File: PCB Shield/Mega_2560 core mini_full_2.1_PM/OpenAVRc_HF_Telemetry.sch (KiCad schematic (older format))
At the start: 12 parts, among them P18 Ecolage, P19 Module_TX, P20 TTL/RS232, P7 SPIX, U1 74LVC1G3157GV, U2 TLP290, U3 TLP290

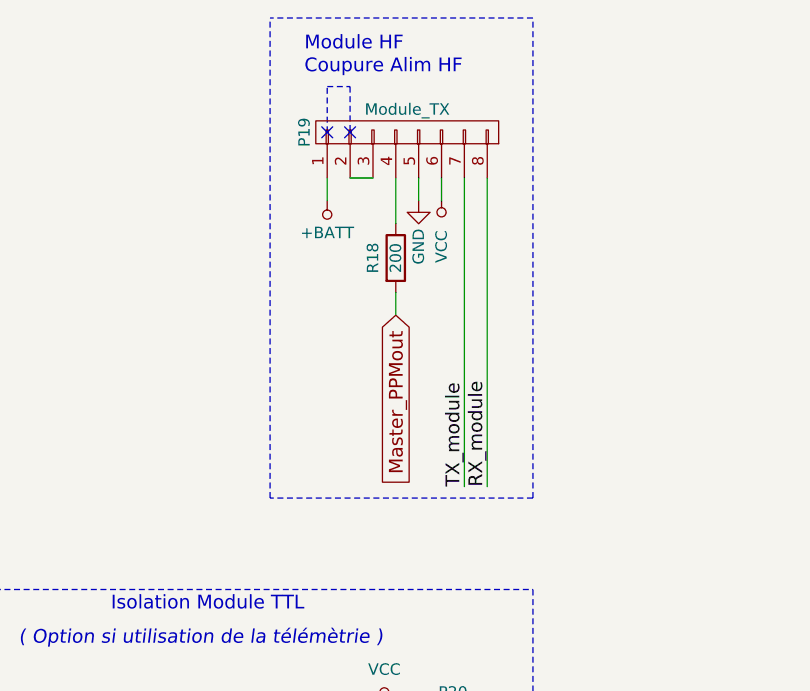
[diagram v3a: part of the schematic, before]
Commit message: Update schematic & pcb
-modify P19 pinout
-connect Q1 to B7 pin's core
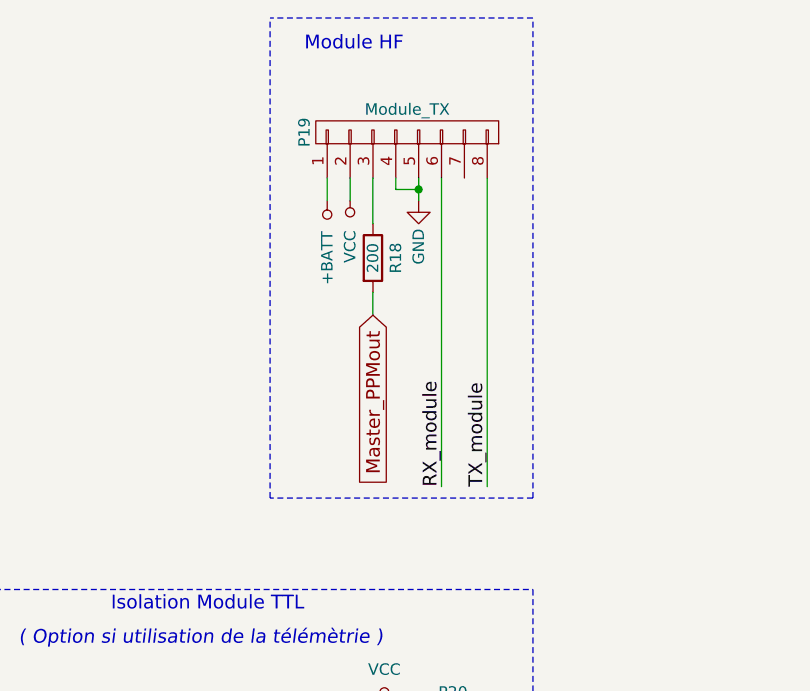
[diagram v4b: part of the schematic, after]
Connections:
- net GND: now also P19.4 (P4)
- net RX_module: now also P19.6 (P6); no longer P19.8 (P8)
- net TX_module: now also P19.8 (P8); no longer P19.7 (P7)
- net VCC: now also P19.2 (P2); no longer P19.6 (P6)
- net at P19.3 (P3): now also R18.1; no longer P19.2 (P2)
- no-connect marks 2 -> 0
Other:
- note removed: "Coupure Alim HF"
- moved on the sheet: R18
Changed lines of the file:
@@
 Sheet 4 7
 Title "Shield Mega2560 core Full"
-Date "2018-02-03"
+Date "2018-02-14"
 Rev "2.10"
 Comp "© Team OpenAVRc"
@@
 $EndComp
 $Comp
-L GND-RESCUE-Mega_2560_core_mini_full_2.0 #PWR66
+L GND-RESCUE-Mega_2560_core_mini_full_2.0 #PWR067
 U 1 1 59C6B422
 P 1850 5200
-F 0 "#PWR66" H 1850 4950 50  0001 C CNN
+F 0 "#PWR067" H 1850 4950 50  0001 C CNN
 F 1 "GND" H 1850 5050 50  0000 C CNN
 F 2 "" H 1850 5200 50  0000 C CNN
@@
 $EndComp
 $Comp
-L +BATT #PWR65
+L +BATT #PWR068
 U 1 1 59C6B429
 P 1600 4100
-F 0 "#PWR65" H 1600 3950 50  0001 C CNN
+F 0 "#PWR068" H 1600 3950 50  0001 C CNN
 F 1 "+BATT" H 1600 4240 50  0000 C CNN
 F 2 "" H 1600 4100 50  0000 C CNN
@@
 $EndComp
 $Comp
-L GND-RESCUE-Mega_2560_core_mini_full_2.0 #PWR70
+L GND-RESCUE-Mega_2560_core_mini_full_2.0 #PWR069
 U 1 1 59C6B436
 P 3850 2000
-F 0 "#PWR70" H 3850 1750 50  0001 C CNN
+F 0 "#PWR069" H 3850 1750 50  0001 C CNN
 F 1 "GND" V 3850 1800 50  0000 C CNN
 F 2 "" H 3850 2000 50  0000 C CNN
@@
 $EndComp
 $Comp
-L VCC #PWR71
+L VCC #PWR070
 U 1 1 59C6B43D
-P 3950 2000
-F 0 "#PWR71" H 3950 1850 50  0001 C CNN
-F 1 "VCC" V 3950 2200 50  0000 C CNN
-F 2 "" H 3950 2000 50  0000 C CNN
-F 3 "" H 3950 2000 50  0000 C CNN
-	1    3950 2000
+P 3550 2000
+F 0 "#PWR070" H 3550 1850 50  0001 C CNN
+F 1 "VCC" V 3550 2200 50  0000 C CNN
+F 2 "" H 3550 2000 50  0000 C CNN
+F 3 "" H 3550 2000 50  0000 C CNN
+	1    3550 2000
 	-1   0    0    1
 $EndComp
@@
 Isolation Module TTL
 $Comp
-L +BATT #PWR67
+L +BATT #PWR071
 U 1 1 59C6B445
 P 3450 2000
-F 0 "#PWR67" H 3450 1850 50  0001 C CNN
-F 1 "+BATT" H 3450 2140 50  0000 C CNN
+F 0 "#PWR071" H 3450 1850 50  0001 C CNN
+F 1 "+BATT" V 3450 2250 50  0000 C CNN
 F 2 "" H 3450 2000 50  0000 C CNN
 F 3 "" H 3450 2000 50  0000 C CNN
@@
 	-1   0    0    1
 $EndComp
-NoConn ~ 3450 1700
-NoConn ~ 3550 1700
 $Comp
 L R-RESCUE-Mega_2560_core_mini_full_2.0 R8
@@
 $EndComp
 $Comp
-L GND-RESCUE-Mega_2560_core_mini_full_2.0 #PWR78
+L GND-RESCUE-Mega_2560_core_mini_full_2.0 #PWR072
 U 1 1 59C6B464
 P 9650 5100
-F 0 "#PWR78" H 9650 4850 50  0001 C CNN
+F 0 "#PWR072" H 9650 4850 50  0001 C CNN
 F 1 "GND" H 9650 4950 50  0000 C CNN
 F 2 "" H 9650 5100 50  0000 C CNN
@@
 $EndComp
 $Comp
-L GND-RESCUE-Mega_2560_core_mini_full_2.0 #PWR69
+L GND-RESCUE-Mega_2560_core_mini_full_2.0 #PWR073
 U 1 1 59C6B478
 P 3750 5000
-F 0 "#PWR69" H 3750 4750 50  0001 C CNN
+F 0 "#PWR073" H 3750 4750 50  0001 C CNN
 F 1 "GND" H 3750 4850 50  0000 C CNN
 F 2 "" H 3750 5000 50  0000 C CNN
@@
 $EndComp
 $Comp
-L VCC #PWR68
+L VCC #PWR074
 U 1 1 59C6B47E
 P 3700 4200
-F 0 "#PWR68" H 3700 4050 50  0001 C CNN
+F 0 "#PWR074" H 3700 4050 50  0001 C CNN
 F 1 "VCC" H 3700 4350 50  0000 C CNN
 F 2 "" H 3700 4200 50  0000 C CNN
@@
 	1    0    0    -1
 $EndComp
-Text Notes 3350 1450 0    60   ~ 0
-Coupure Alim HF
 Text Label 3200 4350 0    60   ~ 0
 TX_module
@@
 RX_module
 Text Label 4150 3250 1    60   ~ 0
+TX_module
+Text Label 3950 3250 1    60   ~ 0
 RX_module
-Text Label 4050 3250 1    60   ~ 0
-TX_module
 $Comp
 L 74LVC1G3157 U1
@@
 $EndComp
 $Comp
-L VCC #PWR77
+L VCC #PWR075
 U 1 1 59C6B497
 P 8800 4500
-F 0 "#PWR77" H 8800 4350 50  0001 C CNN
+F 0 "#PWR075" H 8800 4350 50  0001 C CNN
 F 1 "VCC" H 8800 4650 50  0000 C CNN
 F 2 "" H 8800 4500 50  0000 C CNN
@@
 $EndComp
 $Comp
-L GND-RESCUE-Mega_2560_core_mini_full_2.0 #PWR75
+L GND-RESCUE-Mega_2560_core_mini_full_2.0 #PWR076
 U 1 1 59C6B49D
 P 7350 4500
-F 0 "#PWR75" H 7350 4250 50  0001 C CNN
+F 0 "#PWR076" H 7350 4250 50  0001 C CNN
 F 1 "GND" H 7350 4350 50  0000 C CNN
 F 2 "" H 7350 4500 50  0000 C CNN
@@
 Wire Notes Line
 	1450 5450 4350 5450
-Wire Wire Line
-	3650 1900 3550 1900
 Connection ~ 1850 5000
 Wire Wire Line
@@
 	4150 1900 4150 3250
 Wire Wire Line
-	4050 1900 4050 3250
+	3950 1900 3950 3250
 Wire Wire Line
 	3750 4550 3800 4550
@@
 	1450 5450 1450 3700
 Wire Notes Line
-	3450 1700 3450 1500
-Wire Notes Line
-	3450 1500 3550 1500
-Wire Notes Line
-	3550 1500 3550 1700
-Wire Notes Line
 	4350 1200 3200 1200
 Wire Wire Line
@@
 Wire Wire Line
 	3750 4950 3800 4950
-Wire Wire Line
-	3950 2000 3950 1900
 Wire Wire Line
 	3850 2000 3850 1900
@@
 $EndComp
 $Comp
-L GND-RESCUE-Mega_2560_core_mini_full_2.0 #PWR76
+L GND-RESCUE-Mega_2560_core_mini_full_2.0 #PWR077
 U 1 1 59C6C686
 P 7550 2200
-F 0 "#PWR76" H 7550 1950 50  0001 C CNN
+F 0 "#PWR077" H 7550 1950 50  0001 C CNN
 F 1 "GND" H 7550 2050 50  0000 C CNN
 F 2 "" H 7550 2200 50  0000 C CNN
@@
 $EndComp
 $Comp
-L GND-RESCUE-Mega_2560_core_mini_full_2.0 #PWR73
+L GND-RESCUE-Mega_2560_core_mini_full_2.0 #PWR078
 U 1 1 59C6C68C
 P 7250 1850
-F 0 "#PWR73" H 7250 1600 50  0001 C CNN
+F 0 "#PWR078" H 7250 1600 50  0001 C CNN
 F 1 "GND" H 7250 1700 50  0000 C CNN
 F 2 "" H 7250 1850 50  0000 C CNN
@@
 $EndComp
 $Comp
-L VCC #PWR74
+L VCC #PWR079
 U 1 1 59C6C694
 P 7350 2000
-F 0 "#PWR74" H 7350 1850 50  0001 C CNN
+F 0 "#PWR079" H 7350 1850 50  0001 C CNN
 F 1 "VCC" V 7350 2150 50  0000 C CNN
 F 2 "" H 7350 2000 50  0000 C CNN
@@
 Sim_control
 $Comp
-L +3,3V #PWR72
+L +3,3V #PWR080
 U 1 1 59CA7757
 P 7050 1950
-F 0 "#PWR72" H 7050 1910 30  0001 C CNN
+F 0 "#PWR080" H 7050 1910 30  0001 C CNN
 F 1 "+3,3V" V 7050 2150 39  0000 C CNN
 F 2 "" H 7050 1950 60  0001 C CNN
@@
 L R-RESCUE-Mega_2560_core_mini_full_2.0 R18
 U 1 1 5A718C98
-P 3750 2250
-F 0 "R18" V 3650 2250 50  0000 C CNN
-F 1 "200" V 3750 2250 50  0000 C CNN
-F 2 "Resistors_SMD:R_1206" V 3680 2250 50  0001 C CNN
-F 3 "" H 3750 2250 50  0000 C CNN
-	1    3750 2250
-	1    0    0    -1
-$EndComp
-Wire Wire Line
-	3750 2100 3750 1900
+P 3650 2250
+F 0 "R18" V 3750 2250 50  0000 C CNN
+F 1 "200" V 3650 2250 50  0000 C CNN
+F 2 "Resistors_SMD:R_1206" V 3580 2250 50  0001 C CNN
+F 3 "" H 3650 2250 50  0000 C CNN
+	1    3650 2250
+	1    0    0    -1
+$EndComp
 $Comp
 L R-RESCUE-Mega_2560_core_mini_full_2.0 R19
@@
 Wire Wire Line
 	2650 5000 2550 5000
-Text GLabel 3750 2500 3    60   Input ~ 0
+Text GLabel 3650 2500 3    60   Input ~ 0
 Master_PPMout
 Wire Wire Line
-	3750 2500 3750 2400
+	3650 2500 3650 2400
 Wire Notes Line
 	4350 3300 3200 3300
@@
 Wire Notes Line
 	3200 3300 3200 1200
+Wire Wire Line
+	3650 2100 3650 1900
+Connection ~ 3850 1950
+Wire Wire Line
+	3550 2000 3550 1900
+Wire Wire Line
+	3750 1900 3750 1950
+Wire Wire Line
+	3750 1950 3850 1950
 $EndSCHEMATC

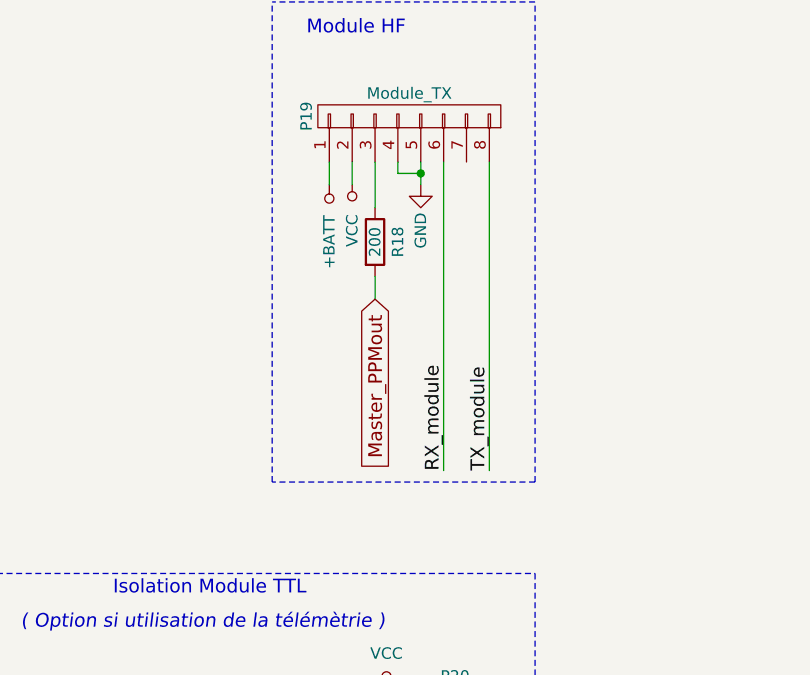
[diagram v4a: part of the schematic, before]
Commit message: Update schemtaic & PCB files
-update P19 pinout .
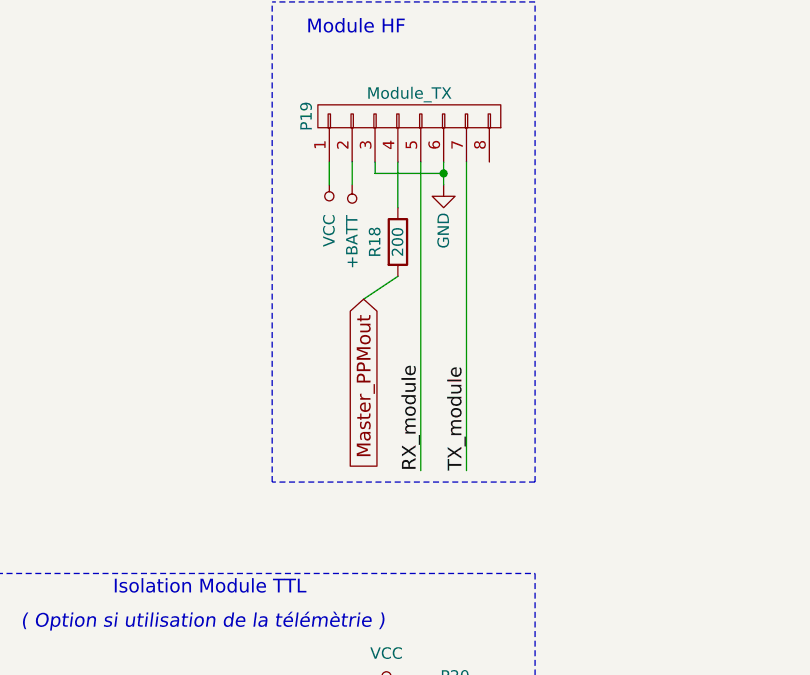
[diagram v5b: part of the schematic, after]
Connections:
- net +BATT: now also P19.2 (P2); no longer P19.1 (P1)
- net GND: now also P19.3 (P3), P19.6 (P6); no longer P19.4 (P4), P19.5 (P5)
- net RX_module: now also P19.5 (P5); no longer P19.6 (P6)
- net TX_module: now also P19.7 (P7); no longer P19.8 (P8)
- net VCC: now also P19.1 (P1); no longer P19.2 (P2)
- net at R18.1: now also P19.4 (P4); no longer P19.3 (P3)
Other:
- moved on the sheet: R18
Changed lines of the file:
@@
 Sheet 4 7
 Title "Shield Mega2560 core Full"
-Date "2018-02-14"
+Date "2018-02-15"
 Rev "2.10"
 Comp "© Team OpenAVRc"
@@
 L GND-RESCUE-Mega_2560_core_mini_full_2.0 #PWR069
 U 1 1 59C6B436
-P 3850 2000
-F 0 "#PWR069" H 3850 1750 50  0001 C CNN
-F 1 "GND" V 3850 1800 50  0000 C CNN
-F 2 "" H 3850 2000 50  0000 C CNN
-F 3 "" H 3850 2000 50  0000 C CNN
-	1    3850 2000
+P 3950 2000
+F 0 "#PWR069" H 3950 1750 50  0001 C CNN
+F 1 "GND" V 3950 1800 50  0000 C CNN
+F 2 "" H 3950 2000 50  0000 C CNN
+F 3 "" H 3950 2000 50  0000 C CNN
+	1    3950 2000
 	1    0    0    -1
 $EndComp
@@
 L VCC #PWR070
 U 1 1 59C6B43D
+P 3450 2000
+F 0 "#PWR070" H 3450 1850 50  0001 C CNN
+F 1 "VCC" V 3450 2200 50  0000 C CNN
+F 2 "" H 3450 2000 50  0000 C CNN
+F 3 "" H 3450 2000 50  0000 C CNN
+	1    3450 2000
+	-1   0    0    1
+$EndComp
+Text Notes 3350 3800 2    60   ~ 0
+Isolation Module TTL
+$Comp
+L +BATT #PWR071
+U 1 1 59C6B445
 P 3550 2000
-F 0 "#PWR070" H 3550 1850 50  0001 C CNN
-F 1 "VCC" V 3550 2200 50  0000 C CNN
+F 0 "#PWR071" H 3550 1850 50  0001 C CNN
+F 1 "+BATT" V 3550 2250 50  0000 C CNN
 F 2 "" H 3550 2000 50  0000 C CNN
 F 3 "" H 3550 2000 50  0000 C CNN
 	1    3550 2000
-	-1   0    0    1
-$EndComp
-Text Notes 3350 3800 2    60   ~ 0
-Isolation Module TTL
-$Comp
-L +BATT #PWR071
-U 1 1 59C6B445
-P 3450 2000
-F 0 "#PWR071" H 3450 1850 50  0001 C CNN
-F 1 "+BATT" V 3450 2250 50  0000 C CNN
-F 2 "" H 3450 2000 50  0000 C CNN
-F 3 "" H 3450 2000 50  0000 C CNN
-	1    3450 2000
 	-1   0    0    1
 $EndComp
@@
 Text Label 3200 4250 0    60   ~ 0
 RX_module
-Text Label 4150 3250 1    60   ~ 0
+Text Label 4050 3250 1    60   ~ 0
 TX_module
-Text Label 3950 3250 1    60   ~ 0
+Text Label 3850 3250 1    60   ~ 0
 RX_module
 $Comp
@@
 	2600 4300 2550 4300
 Wire Wire Line
-	4150 1900 4150 3250
-Wire Wire Line
-	3950 1900 3950 3250
+	4050 1900 4050 3250
+Wire Wire Line
+	3850 1900 3850 3250
 Wire Wire Line
 	3750 4550 3800 4550
@@
 	3750 4950 3800 4950
 Wire Wire Line
-	3850 2000 3850 1900
-Wire Wire Line
-	3450 2000 3450 1900
+	3550 2000 3550 1900
 $Comp
 L C-RESCUE-Mega_2560_core_mini_full_2.0 C6
@@
 L R-RESCUE-Mega_2560_core_mini_full_2.0 R18
 U 1 1 5A718C98
-P 3650 2250
-F 0 "R18" V 3750 2250 50  0000 C CNN
-F 1 "200" V 3650 2250 50  0000 C CNN
-F 2 "Resistors_SMD:R_1206" V 3580 2250 50  0001 C CNN
-F 3 "" H 3650 2250 50  0000 C CNN
-	1    3650 2250
+P 3750 2250
+F 0 "R18" V 3650 2250 50  0000 C CNN
+F 1 "200" V 3750 2250 50  0000 C CNN
+F 2 "Resistors_SMD:R_1206" V 3680 2250 50  0001 C CNN
+F 3 "" H 3750 2250 50  0000 C CNN
+	1    3750 2250
 	1    0    0    -1
 $EndComp
@@
 Wire Wire Line
 	2650 5000 2550 5000
-Text GLabel 3650 2500 3    60   Input ~ 0
+Text GLabel 3600 2500 3    60   Input ~ 0
 Master_PPMout
 Wire Wire Line
-	3650 2500 3650 2400
+	3600 2500 3750 2400
 Wire Notes Line
 	4350 3300 3200 3300
@@
 	3200 3300 3200 1200
 Wire Wire Line
-	3650 2100 3650 1900
-Connection ~ 3850 1950
-Wire Wire Line
-	3550 2000 3550 1900
-Wire Wire Line
-	3750 1900 3750 1950
-Wire Wire Line
-	3750 1950 3850 1950
+	3750 2100 3750 1900
+Wire Wire Line
+	3450 2000 3450 1900
+Wire Wire Line
+	3650 1950 3950 1950
+Wire Wire Line
+	3950 1900 3950 2000
+Connection ~ 3950 1950
+Wire Wire Line
+	3650 1950 3650 1900
 $EndSCHEMATC

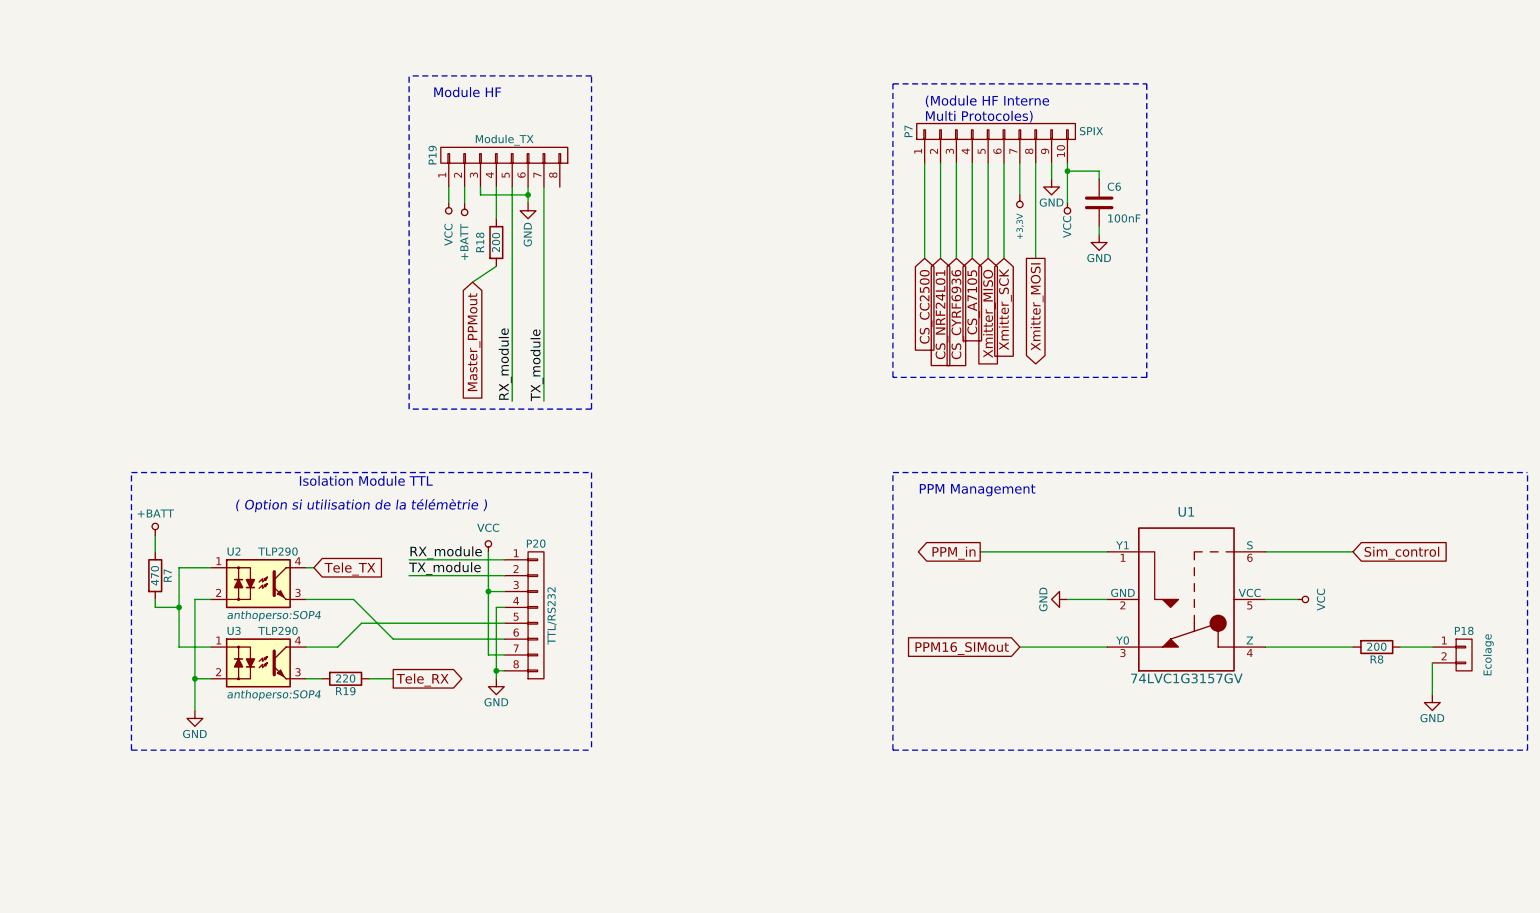
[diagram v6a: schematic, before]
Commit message: Update schematic é pcb files
-replace u2 and u3 by 2 74lvc1g3157gv
-remove p15 and p3
-add ftdi connector as p3
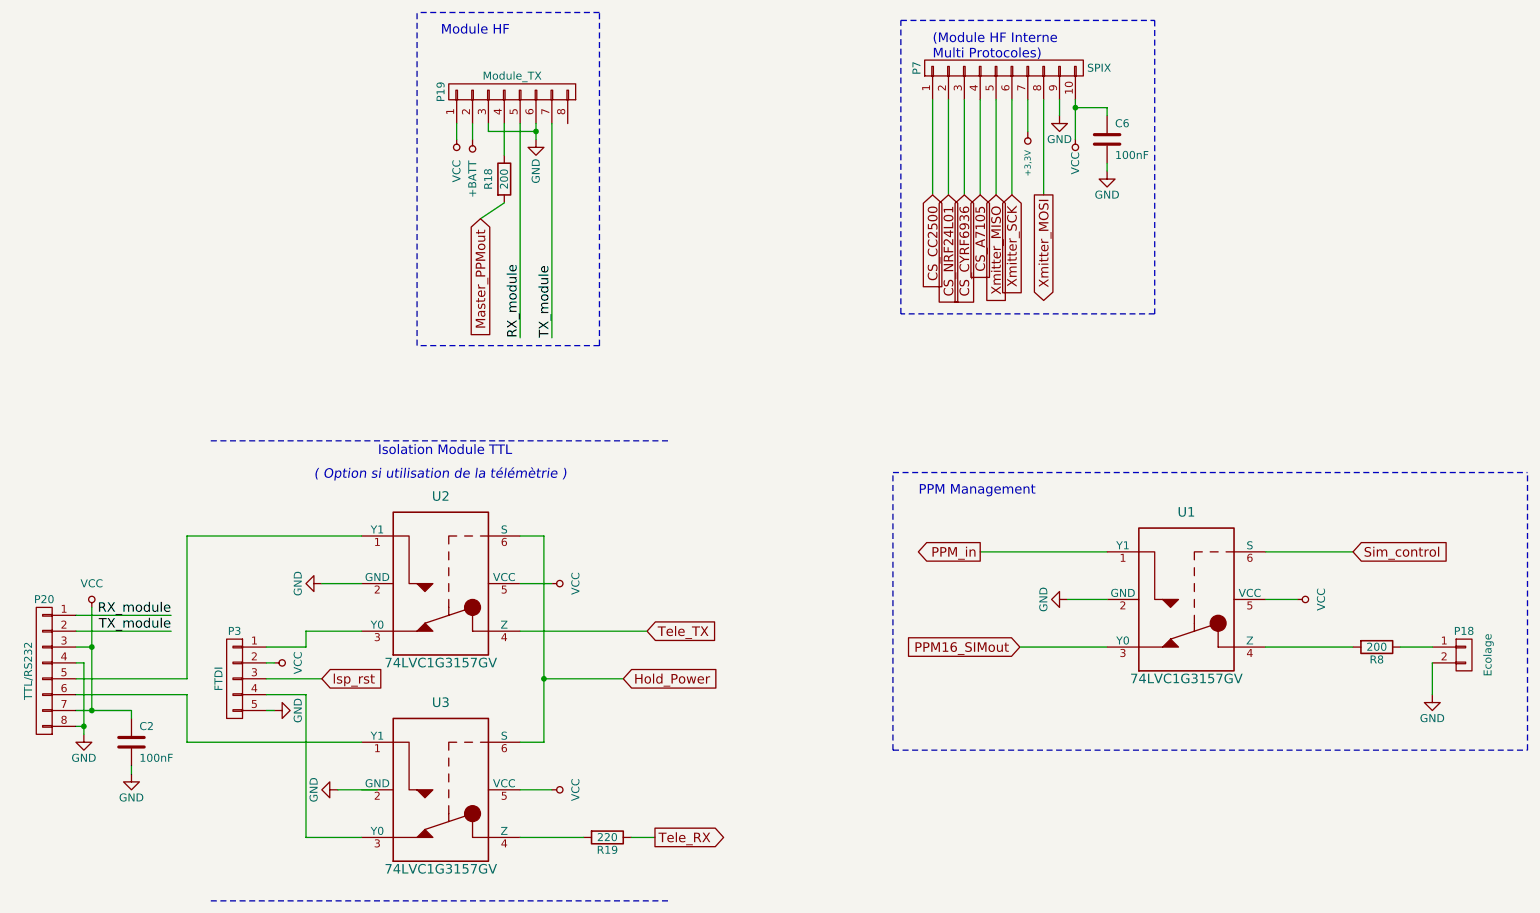
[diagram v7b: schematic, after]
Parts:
- removed R7: 470, Resistors_SMD:R_1206, symbol R-RESCUE-Mega_2560_core_mini_full_2.0
- removed U2, U3: TLP290, anthoperso:SOP4, symbol TLP290-RESCUE-Mega_2560_core_mini_full_2.0
- added C2: 100nF, Capacitors_SMD:C_1206, symbol C-RESCUE-Mega_2560_core_mini_full_2.0
- added P3: FTDI, symbol CONN_01X05
- added U2, U3: 74LVC1G3157GV, SOT-457, symbol 74LVC1G3157
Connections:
- net GND: now also C2.2, P3.5 (P5), U2.2 (GND)
- net Tele_TX: now also U2.4 (Z)
- net VCC: now also C2.1, P3.2 (P2), U2.5 (VCC), U3.5 (VCC)
- net at R19.2: now also U3.4 (Z)
- net at P20.5 (P5): now also U2.1 (Y1)
- net at P20.6 (P6): now also U3.1 (Y1)
- new net: P3.1 (P1), U2.3 (Y0)
- new net: P3.4 (P4), U3.3 (Y0)
- new net Hold_Power: U2.6 (S), U3.6 (S)
- new net lsp_rst: P3.3 (P3)
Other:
- moved on the sheet: C6, P19, P20, P7, R18, R19
